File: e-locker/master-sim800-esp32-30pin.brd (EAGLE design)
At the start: 100 x 100 mm, 59 parts, among them T1 BC847, T2 BC847, T3 BC847, T4 BC847, U1 AT24C128C-SSHM-T, X1 JST-XH-02-PIN-LONG-PAD, X10 JST-XH-05-PIN-LONG-PAD, X11 JST-XH-02-PIN-LONG-PAD, X12 JST-XH-02-PIN-LONG-PAD, X13 JST-XH-02-PIN-LONG-PAD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

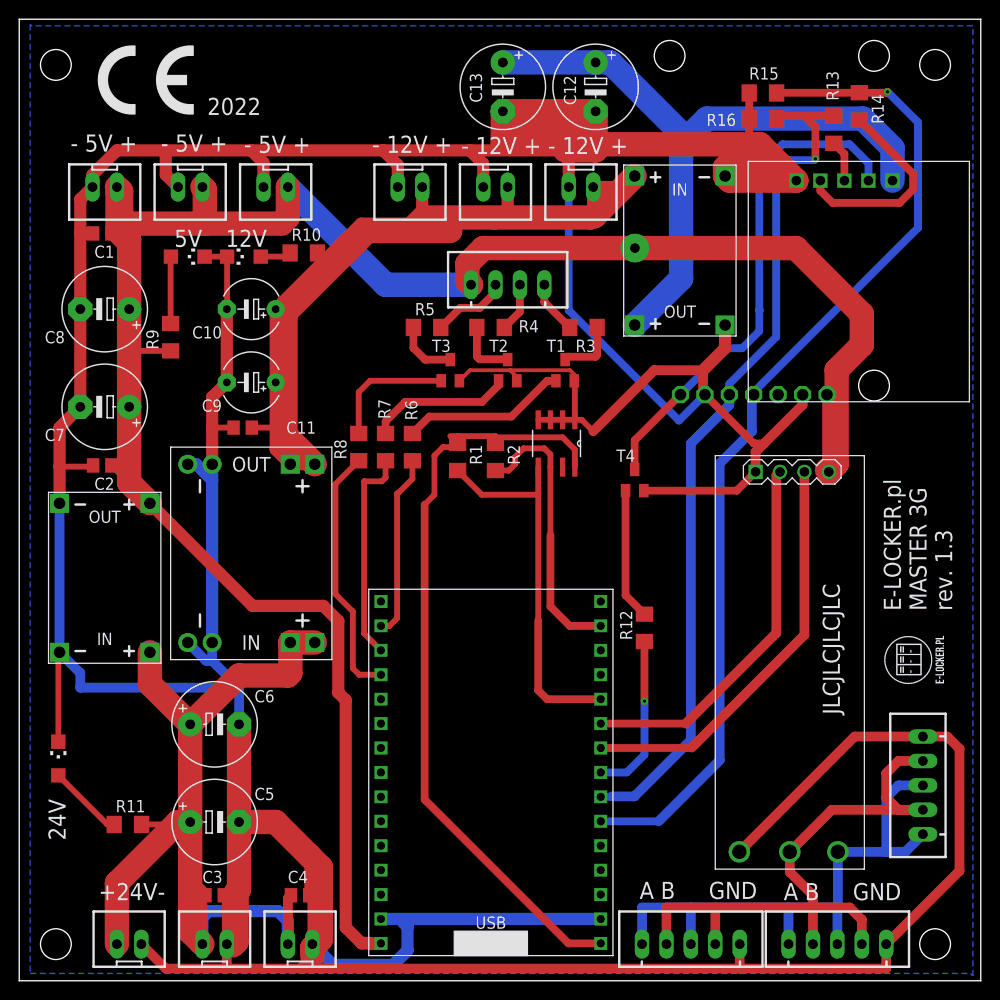
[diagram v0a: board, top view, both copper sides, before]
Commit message: ESP32 footprint change
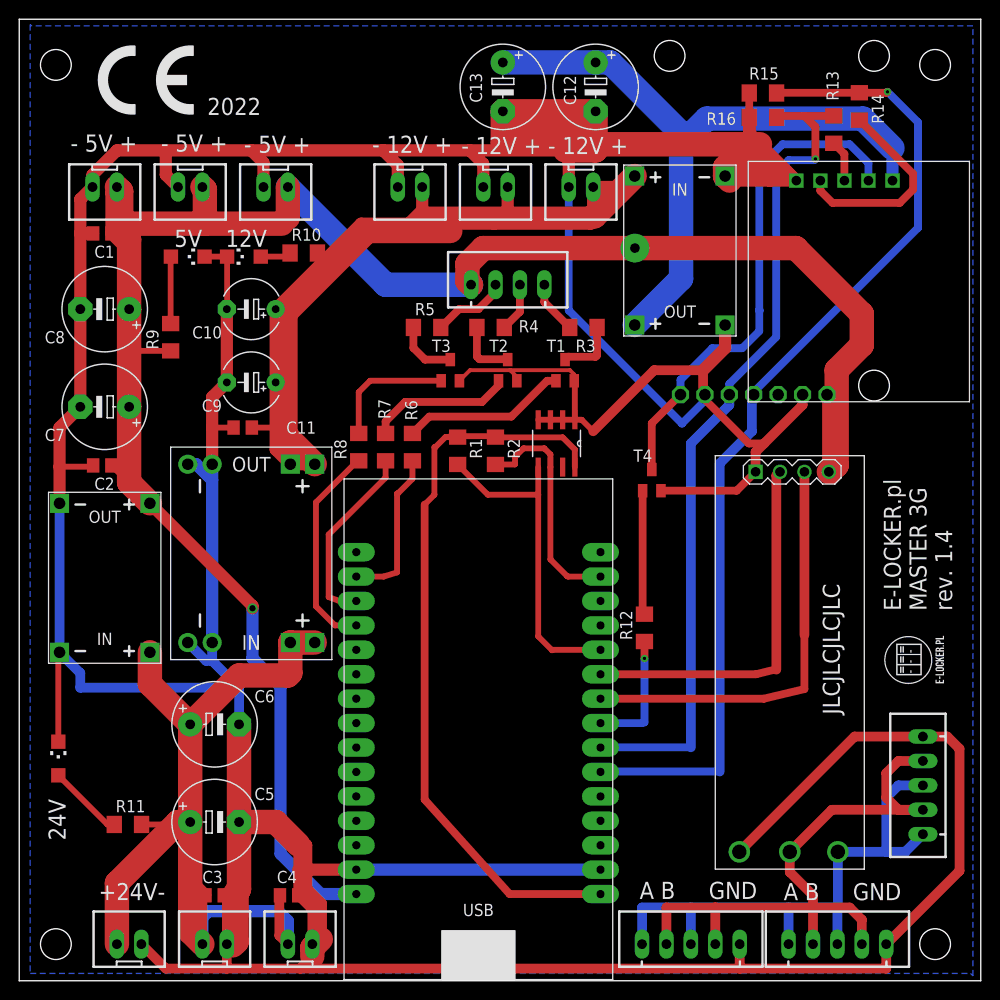
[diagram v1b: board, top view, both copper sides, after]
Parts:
- moved U$1 5.74 mm to (33.8, 7.75)
- moved T4 1.78 mm to (65.8, 52.1)
- moved C4 1.14 mm to (28.1, 8.89)
- moved R1 0.64 mm to (45.6, 55.1)
- moved R2 0.64 mm to (49.5, 55.1)
- moved R16 0.13 mm to (77.3, 89.8)
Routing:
- net VCC: track 264.5 -> 254.8 mm, vias 0 -> 1
- net GND: track 657.2 -> 665.3 mm
- net N$2: track 29.3 -> 24.0 mm
- net N$8: track 39.5 -> 34.4 mm
- net G34: track 26.5 -> 22.1 mm
- net N$24: track 17.1 -> 13.0 mm
- net G39: track 22.4 -> 19.6 mm
- net G36: track 19.1 -> 16.6 mm
- net V33: track 80.4 -> 78.1 mm
- net N$4: track 90.2 -> 88.5 mm
- net N$3: track 106.0 -> 104.5 mm
- net N$6: track 43.0 -> 43.9 mm
- net N$25: track 13.7 -> 12.9 mm
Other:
- board text added: "E-LOCKER.pl MASTER 3G rev. 1.4"
- board text removed: "E-LOCKER.pl MASTER 3G rev. 1.3"

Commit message: fixes
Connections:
- new net G25: R8.1, U$1.GPIO25
- new net G26: R7.1, U$1.GPIO26
- new net G27: R6.1, U$1.GPIO27
- net G34: no longer R8.1
- net G36: no longer R6.1
- net G39: no longer R7.1
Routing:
- net G27: track 0.00 -> 36.9 mm
- net G26: track 0.00 -> 33.6 mm
- net G25: track 0.00 -> 30.7 mm
- net G34: track 22.1 -> 0.00 mm
- net G39: track 19.6 -> 0.00 mm
- net G36: track 16.6 -> 0.00 mm
- net V33: track 78.1 -> 77.3 mm
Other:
- board text added: "E-LOCKER.pl MASTER 3G rev. 1.5"
- board text removed: "E-LOCKER.pl MASTER 3G rev. 1.4"
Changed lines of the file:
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@@
 <text x="97.028" y="38.481" size="1.778" layer="25" rot="R90">E-LOCKER.pl
 MASTER 3G
-rev. 1.4</text>
+rev. 1.5</text>
 <text x="5.334" y="86.233" size="1.778" layer="25">- 5V +</text>
 <text x="14.732" y="86.233" size="1.778" layer="25">- 5V +</text>
@@
 <wire x1="44.323" y1="56.54" x2="43.282" y2="55.499" width="0.6096" layer="1"/>
 <wire x1="43.282" y1="55.499" x2="43.18" y2="55.499" width="0.6096" layer="1"/>
-<wire x1="43.18" y1="55.499" x2="43.18" y2="50.546" width="0.6096" layer="1"/>
-<wire x1="42.164" y1="49.53" x2="43.18" y2="50.546" width="0.6096" layer="1"/>
 <wire x1="60.452" y1="9.017" x2="51.00365" y2="9.017" width="0.8128" layer="1"/>
-<wire x1="51.00365" y1="9.017" x2="42.164" y2="18.8468" width="0.8128" layer="1"/>
-<wire x1="42.164" y1="18.8468" x2="42.164" y2="49.53" width="0.8128" layer="1"/>
+<wire x1="51.00365" y1="9.017" x2="43.18" y2="17.716996875" width="0.8128" layer="1"/>
+<wire x1="43.18" y1="17.716996875" x2="43.18" y2="55.499" width="0.8128" layer="1"/>
 </signal>
 <signal name="N$9">
@@
 </signal>
 <signal name="G36">
-<contactref element="R6" pad="1"/>
 <contactref element="U$1" pad="GPIO36"/>
-<wire x1="40.894" y1="54.077" x2="40.894" y2="52.197" width="0.6096" layer="1"/>
-<wire x1="40.894" y1="52.197" x2="39.37" y2="50.673" width="0.6096" layer="1"/>
-<wire x1="39.37" y1="50.673" x2="39.2938" y2="50.673" width="0.6096" layer="1"/>
-<wire x1="39.2938" y1="50.673" x2="39.2938" y2="42.4730125" width="0.6096" layer="1"/>
-<wire x1="35.052" y1="42.037" x2="37.89798125" y2="42.037" width="0.6096" layer="1"/>
-<wire x1="39.2938" y1="42.4730125" x2="37.89798125" y2="42.037" width="0.6096" layer="1"/>
 </signal>
 <signal name="G39">
-<contactref element="R7" pad="1"/>
 <contactref element="U$1" pad="GPIO39"/>
-<wire x1="38.1" y1="54.077" x2="38.1" y2="52.324" width="0.6096" layer="1"/>
-<wire x1="32.1818" y1="46.4058" x2="32.1818" y2="39.90458125" width="0.6096" layer="1"/>
-<wire x1="35.052" y1="39.497" x2="33.3038625" y2="39.497" width="0.6096" layer="1"/>
-<wire x1="33.3038625" y1="39.497" x2="32.1818" y2="39.90458125" width="0.6096" layer="1"/>
-<wire x1="38.1" y1="52.324" x2="32.1818" y2="46.4058" width="0.6096" layer="1"/>
 </signal>
 <signal name="G34">
-<contactref element="R8" pad="1"/>
 <contactref element="U$1" pad="GPIO34"/>
-<wire x1="35.306" y1="54.077" x2="35.179" y2="54.077" width="0.6096" layer="1"/>
-<wire x1="35.179" y1="54.077" x2="30.861" y2="49.759" width="0.6096" layer="1"/>
-<wire x1="30.861" y1="49.759" x2="30.861" y2="38.9382" width="0.6096" layer="1"/>
-<wire x1="35.052" y1="36.957" x2="32.8422" y2="36.957" width="0.6096" layer="1"/>
-<wire x1="32.8422" y1="36.957" x2="30.861" y2="38.9382" width="0.6096" layer="1"/>
 </signal>
 <signal name="N$5">
@@
 <via x="64.0334" y="76.2" extent="1-16" drill="1" diameter="3" shape="square"/>
 </signal>
+<signal name="G25">
+<contactref element="U$1" pad="GPIO25"/>
+<contactref element="R8" pad="1"/>
+<wire x1="35.306" y1="54.077" x2="35.306" y2="50.292" width="0.8128" layer="1"/>
+<wire x1="37.9222" y1="47.6758" x2="37.9222" y2="27.686" width="0.8128" layer="1"/>
+<wire x1="37.9222" y1="27.686" x2="37.0332" y2="26.797" width="0.8128" layer="1"/>
+<wire x1="37.0332" y1="26.797" x2="35.052" y2="26.797" width="0.8128" layer="1"/>
+<wire x1="35.306" y1="50.292" x2="37.9222" y2="47.6758" width="0.8128" layer="1"/>
+</signal>
+<signal name="G26">
+<contactref element="U$1" pad="GPIO26"/>
+<contactref element="R7" pad="1"/>
+<wire x1="38.1" y1="54.077" x2="38.1" y2="52.578" width="0.8128" layer="1"/>
+<wire x1="38.1" y1="52.578" x2="39.243" y2="51.435" width="0.8128" layer="1"/>
+<wire x1="39.243" y1="51.435" x2="39.243" y2="25.781" width="0.8128" layer="1"/>
+<wire x1="37.719" y1="24.257" x2="35.052" y2="24.257" width="0.8128" layer="1"/>
+<wire x1="39.243" y1="25.781" x2="37.719" y2="24.257" width="0.8128" layer="1"/>
+</signal>
+<signal name="G27">
+<contactref element="U$1" pad="GPIO27"/>
+<contactref element="R6" pad="1"/>
+<wire x1="40.894" y1="54.077" x2="40.894" y2="24.003" width="0.8128" layer="1"/>
+<wire x1="40.894" y1="24.003" x2="38.608" y2="21.717" width="0.8128" layer="1"/>
+<wire x1="38.608" y1="21.717" x2="35.052" y2="21.717" width="0.8128" layer="1"/>
+</signal>
 </signals>

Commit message: QR code reader header
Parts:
- added X14: JST-XH-04-PIN-LONG-PAD, Rembrandt Electronics - JST XH Connectors v1-0:JST-XH-04-PACKAGE-LONG-PAD
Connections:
- new net N$30: U$1.GPIO13, X14.3
- new net N$31: U$1.GPIO12, X14.4
- net GND: now also X14.1
- net VCC: now also X14.2
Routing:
- net N$31: track 0.00 -> 13.5 mm
- net N$30: track 0.00 -> 12.8 mm
- net VCC: track 254.8 -> 257.4 mm
- net GND: track 665.3 -> 667.7 mm
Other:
- board text added: "E-LOCKER.pl MASTER 3G rev. 1.6"
- board text removed: "E-LOCKER.pl MASTER 3G rev. 1.5"
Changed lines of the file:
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@@
 <text x="97.028" y="38.481" size="1.778" layer="25" rot="R90">E-LOCKER.pl
 MASTER 3G
-rev. 1.5</text>
+rev. 1.6</text>
 <text x="5.334" y="86.233" size="1.778" layer="25">- 5V +</text>
 <text x="14.732" y="86.233" size="1.778" layer="25">- 5V +</text>
@@
 </element>
 <element name="C5" library="adafruit" library_urn="urn:adsk.eagle:library:420" package="E5-8,5" package3d_urn="urn:adsk.eagle:package:6240526/1" value="" x="20.32" y="16.51" smashed="yes">
-<attribute name="NAME" x="24.4602" y="18.796" size="1.27" layer="25" ratio="10"/>
+<attribute name="NAME" x="13.4112" y="19.05" size="1.27" layer="25" ratio="10"/>
 <attribute name="VALUE" x="17.8054" y="13.4874" size="1.27" layer="27" ratio="10"/>
 </element>
 <element name="C6" library="adafruit" library_urn="urn:adsk.eagle:library:420" package="E5-8,5" package3d_urn="urn:adsk.eagle:package:6240526/1" value="" x="20.32" y="26.67" smashed="yes">
-<attribute name="NAME" x="24.4602" y="28.956" size="1.27" layer="25" ratio="10"/>
+<attribute name="NAME" x="13.2842" y="25.273" size="1.27" layer="25" ratio="10"/>
 <attribute name="VALUE" x="17.8054" y="23.6474" size="1.27" layer="27" ratio="10"/>
 </element>
@@
 </element>
 <element name="U$9" library="logo" library_urn="urn:adsk.eagle:library:264" package="CE_7.3MM" value="" x="8.128" y="90.043" smashed="yes"/>
+<element name="X14" library="Rembrandt Electronics - JST XH Connectors v1-0" package="JST-XH-04-PACKAGE-LONG-PAD" value="JST-XH-04-PIN-LONG-PAD" x="28.575" y="21.463" smashed="yes" rot="R90">
+<attribute name="NAME" x="30.615" y="14.808" size="1.016" layer="25" ratio="10" rot="R180"/>
+</element>
 </elements>
 <signals>
@@
 <wire x1="35.052" y1="9.017" x2="31.369" y2="9.017" width="1.27" layer="16"/>
 <wire x1="24.257" y1="33.528" x2="24.257" y2="38.735" width="1.27" layer="16"/>
-<wire x1="31.369" y1="9.017" x2="27.178" y2="13.208" width="1.27" layer="16"/>
-<wire x1="27.178" y1="13.208" x2="27.178" y2="30.607" width="1.27" layer="16"/>
-<wire x1="27.178" y1="30.607" x2="24.257" y2="33.528" width="1.27" layer="16"/>
+<wire x1="31.369" y1="9.017" x2="25.908" y2="14.478" width="1.27" layer="16"/>
+<wire x1="25.908" y1="14.478" x2="25.908" y2="20.193" width="1.27" layer="16"/>
+<wire x1="25.908" y1="20.193" x2="25.908" y2="31.877" width="1.27" layer="16"/>
+<wire x1="25.908" y1="31.877" x2="24.257" y2="33.528" width="1.27" layer="16"/>
 <wire x1="84.887" y1="53.617" x2="85.014" y2="53.617" width="1.27" layer="1"/>
 <wire x1="84.887" y1="53.617" x2="84.2" y2="52.93" width="1.27" layer="1"/>
 <wire x1="85.014" y1="53.617" x2="84.327" y2="52.93" width="2.54" layer="1"/>
 <wire x1="84.327" y1="52.93" x2="84.2" y2="52.93" width="2.54" layer="1"/>
+<contactref element="X14" pad="2"/>
+<wire x1="28.575" y1="20.193" x2="25.908" y2="20.193" width="1.016" layer="16"/>
 <wire x1="84.2" y1="52.93" x2="84.01" y2="53.12" width="0" layer="19" extent="1-1"/>
 </signal>
@@
 <wire x1="75.933" y1="88.16005625" x2="77.343" y2="86.75005625" width="1.27" layer="1"/>
 <wire x1="77.343" y1="86.75005625" x2="77.343" y2="86.693" width="1.27" layer="1"/>
+<contactref element="X14" pad="1"/>
+<wire x1="28.575" y1="17.653" x2="27.432" y2="16.51" width="0.6096" layer="1"/>
+<wire x1="27.432" y1="16.51" x2="26.67" y2="16.51" width="0.6096" layer="1"/>
 </signal>
 <signal name="N$2">
@@
 <wire x1="38.608" y1="21.717" x2="35.052" y2="21.717" width="0.8128" layer="1"/>
 </signal>
+<signal name="N$30">
+<contactref element="U$1" pad="GPIO13"/>
+<contactref element="X14" pad="3"/>
+<wire x1="32.3088" y1="15.900525" x2="32.3088" y2="16.0782" width="0.6096" layer="1"/>
+<wire x1="35.052" y1="14.097" x2="34.112325" y2="14.097" width="0.6096" layer="1"/>
+<wire x1="34.112325" y1="14.097" x2="32.3088" y2="15.900525" width="0.6096" layer="1"/>
+<wire x1="31.0134" y1="21.844" x2="30.1244" y2="22.733" width="0.6096" layer="1"/>
+<wire x1="30.1244" y1="22.733" x2="28.575" y2="22.733" width="0.6096" layer="1"/>
+<wire x1="32.3088" y1="16.0782" x2="31.0134" y2="17.3736" width="0.6096" layer="1"/>
+<wire x1="31.0134" y1="17.3736" x2="31.0134" y2="21.844" width="0.6096" layer="1"/>
+</signal>
+<signal name="N$31">
+<contactref element="U$1" pad="GPIO12"/>
+<contactref element="X14" pad="4"/>
+<wire x1="28.575" y1="25.273" x2="30.988" y2="25.273" width="0.6096" layer="1"/>
+<wire x1="32.131" y1="24.13" x2="32.131" y2="18.288" width="0.6096" layer="1"/>
+<wire x1="32.131" y1="18.288" x2="33.782" y2="16.637" width="0.6096" layer="1"/>
+<wire x1="33.782" y1="16.637" x2="35.052" y2="16.637" width="0.6096" layer="1"/>
+<wire x1="30.988" y1="25.273" x2="32.131" y2="24.13" width="0.6096" layer="1"/>
+</signal>
 </signals>

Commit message: v1.7
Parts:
- removed X2, X3, X4: JST-XH-02-PIN-LONG-PAD, Rembrandt Electronics - JST XH Connectors v1-0:JST-XH-02-PACKAGE-LONG-PAD
- added R17, R18: (no value), eagle-ltspice:R1206
- added T5, T6: BC847, transistor:SOT23
- added X15: JST-XH-06-PIN-LONG-PAD, Rembrandt Electronics - JST XH Connectors v1-0:JST-XH-06-PACKAGE-LONG-PAD
- added X16, X17, X18: JST-XH-03-PIN-LONG-PAD, Rembrandt Electronics - JST XH Connectors v1-0:JST-XH-03-PACKAGE-LONG-PAD
- moved U$6 97.4 mm to (19.4, 90.6), turned to 0 degrees
- moved X9 40.0 mm to (94.0, 35.7), turned to 90 degrees
- moved U$1 5.21 mm to (39.0, 8.00)
- moved R8 5.21 mm to (40.5, 55.4)
- moved R7 4.83 mm to (42.9, 55.4)
- moved R6 4.57 mm to (45.5, 55.4)
- moved T4 4.47 mm to (70.2, 52.6)
- moved R12 4.47 mm to (69.3, 37.8)
- moved R1 4.44 mm to (50.0, 55.1)
- moved R11 3.69 mm to (7.62, 16.5)
- moved C5 3.58 mm to (16.8, 16.1)
- moved C6 3.58 mm to (16.8, 26.3)
- moved R2 3.43 mm to (53.0, 55.1)
- moved U1 2.95 mm to (58.8, 56.3)
- moved U$9 2.51 mm to (6.35, 91.8)
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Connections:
- new net N$32: R17.1, T5.1
- new net N$33: R18.1, T6.1
- new net N$34: R18.2, U$1.GPIO32
- new net N$35: T6.3, X15.4
- new net N$36: T5.3, X15.3
- new net N$37: R17.2, U$1.GPIO33
- net GND: now also T5.2, T6.2, X15.2, X16.3, X17.3, X18.3; no longer X2.2, X3.2, X4.2
- net N$23: now also X15.1
- net N$30: now also X15.6
- net N$31: now also U$1.GPIO14, X15.5; no longer U$1.GPIO12
- net VCC: now also X16.1, X17.1, X18.1; no longer X2.1, X3.1, X4.1
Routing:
- net N$36: track 0.00 -> 62.7 mm
- net N$35: track 0.00 -> 52.9 mm, vias 0 -> 1
- net GND: track 667.7 -> 712.8 mm
- net N$37: track 0.00 -> 32.6 mm
- net N$23: track 138.5 -> 168.7 mm
- net N$34: track 0.00 -> 29.1 mm
- net N$19: track 68.5 -> 89.7 mm
- net G27: track 36.9 -> 44.4 mm
- net N$33: track 0.00 -> 6.79 mm
- net VCC: track 257.4 -> 263.8 mm
- net N$30: track 12.8 -> 19.1 mm
- net N$32: track 0.00 -> 6.00 mm
- net N$7: track 39.1 -> 33.8 mm
- net N$6: track 43.9 -> 38.7 mm
- net N$3: track 104.5 -> 99.3 mm
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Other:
- board text added: "+12V"
- board text added: "+5V"
- board text added: "2023"
- board text added: "BUZ"
- board text added: "E-LOCKER.pl MASTER 3G rev. 1.7"
- board text added: "GND"
- board text added: "LED"
- board text added: "RX"
- board text added: "TX"
- board text removed: "2022"
- board text removed: "E-LOCKER.pl MASTER 3G rev. 1.6"
